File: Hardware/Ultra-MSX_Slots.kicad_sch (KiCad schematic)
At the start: 11 parts

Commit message: Finished the VDP-board, finished up the mixer-section, removed the buffer-pins from the FPGA, and instead added external buffers for the slots, designed a marquee-block with the Ultra-MSX logo, designed the logotype, andmultiple other changes.
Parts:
- added R17, R20, R21, R22, R23: R_RC0603FR-0710KL, LRJ:R_0603_1608Metric_roundcourt, symbol LRJ-parts:R_RC0603FR-0710KL
- added U14: SN74ABTH16244DL, Package_SO:TSSOP-56_6.1x14mm_P0.5mm, symbol LRJ-parts:SN74ABTH16244DL
- added U15: SN74ABT241APW, Package_SO:TSSOP-56_6.1x14mm_P0.5mm, symbol LRJ-parts:SN74ABT241APW
- added U6: 74ABT245PW_118, Package_SO:TSSOP-20_4.4x6.5mm_P0.65mm, symbol LRJ-parts:74ABT245PW_118
- R85, R86, R87, R88, R89, R90, R91, R92: footprint Resistor_SMD:R_0603_1608Metric_Pad0.98x0.95mm_HandSolder -> LRJ:R_0603_1608Metric_roundcourt
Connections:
- net +5V: now also R20.2
- net BA0: now also U14.2 (_{1}Y_{1})
- net BA1: now also U14.3 (_{1}Y_{2})
- net BA10: now also U14.16 (_{3}Y_{3})
- net BA11: now also U14.17 (_{3}Y_{4})
- net BA12: now also U14.19 (_{4}Y_{1})
- net BA13: now also U14.20 (_{4}Y_{2})
- net BA14: now also U14.22 (_{4}Y_{3})
- net BA15: now also U14.23 (_{4}Y_{4})
- net BA2: now also U14.5 (_{1}Y_{3})
- net BA3: now also U14.6 (_{1}Y_{4})
- net BA4: now also U14.8 (_{2}Y_{1})
- net BA5: now also U14.9 (_{2}Y_{2})
- net BA6: now also U14.11 (_{2}Y_{3})
- net BA7: now also U14.12 (_{2}Y_{4})
- net BA8: now also U14.13 (_{3}Y_{1})
- net BA9: now also U14.14 (_{3}Y_{2})
- net BD0: now also U6.2 (A0)
- net BD1: now also U6.3 (A1)
- net BD2: now also U6.4 (A2)
- net BD3: now also U6.5 (A3)
- net BD4: now also U6.6 (A4)
- net BD5: now also U6.7 (A5)
- net BD6: now also U6.8 (A6)
- net BD7: now also U6.9 (A7)
- net B_CLK: now also U15.3 (_{2}Y_{4})
- net GND: now also R17.2, R21.2, R22.2, R23.2, U14.24 (4~{OE}), U14.48 (2~{OE})
- net ~{B_IORQ}: now also U15.12 (_{1}Y_{4})
- net ~{B_M1}: now also U15.16 (_{1}Y_{2})
- net ~{B_MREQ}: now also U15.14 (_{1}Y_{3})
- net ~{B_RD}: now also U15.9 (_{2}Y_{1})
- net ~{B_RESET}: now also U15.5 (_{2}Y_{3})
- net ~{B_RFSH}: now also U15.18 (_{1}Y_{1})
- net ~{B_WR}: now also U15.7 (_{2}Y_{2})
- net SLT3_SND renamed SLT3_SND_L
- new net: R23.1, U14.25 (3~{OE})
- new net: R21.1, U6.19 (~{OE})
- new net: R17.1, U15.1 (1~{OE})
- new net: R22.1, U14.1 (1~{OE})
- new net: R20.1, U15.19 (2OE)
- new net A0: U14.47 (_{1}A_{1})
- new net A1: U14.46 (_{1}A_{2})
- new net A10: U14.33 (_{3}A_{3})
- new net A11: U14.32 (_{3}A_{4})
- new net A12: U14.30 (_{4}A_{1})
- new net A13: U14.29 (_{4}A_{2})
- new net A14: U14.27 (_{4}A_{3})
- new net A15: U14.26 (_{4}A_{4})
- new net A2: U14.44 (_{1}A_{3})
- new net A3: U14.43 (_{1}A_{4})
- new net A4: U14.41 (_{2}A_{1})
- new net A5: U14.40 (_{2}A_{2})
- new net A6: U14.38 (_{2}A_{3})
- new net A7: U14.37 (_{2}A_{4})
- new net A8: U14.36 (_{3}A_{1})
- new net A9: U14.35 (_{3}A_{2})
- new net CLK_BUS: U15.17 (_{2}A_{4})
- new net D0: U6.18 (B0)
- new net D1: U6.17 (B1)
- new net D2: U6.16 (B2)
- new net D3: U6.15 (B3)
- new net D4: U6.14 (B4)
- new net D5: U6.13 (B5)
- new net D6: U6.12 (B6)
- new net D7: U6.11 (B7)
- new net SLT_DIR: U6.1 (DIR)
- new net ~{IORQ}: U15.8 (_{1}A_{4})
- new net ~{M1}: U15.4 (_{1}A_{2})
- new net ~{MREQ}: U15.6 (_{1}A_{3})
- new net ~{RD}: U15.11 (_{2}A_{1})
- new net ~{RESET}: U15.15 (_{2}A_{3})
- new net ~{RFSH}: U15.2 (_{1}A_{1})
- new net ~{WR}: U15.13 (_{2}A_{2})
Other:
- note added: "Dual direction buffer"
- note removed: "Buffered Signals"
- moved on the sheet: R85, R86, R87, R88, R89, R90, R91, R92, SLOT1, SLOT2, SLOT3

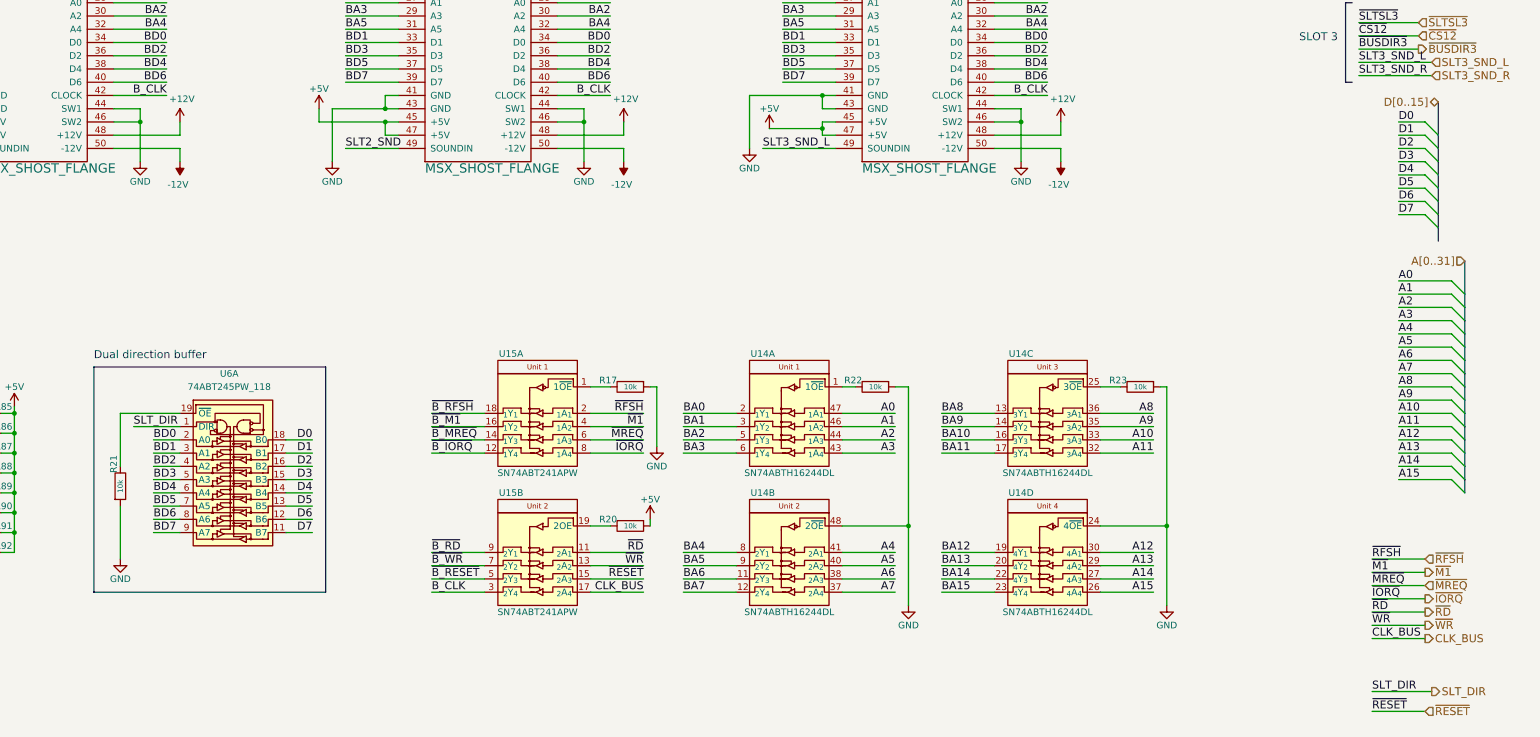
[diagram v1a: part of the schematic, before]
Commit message: Redesigned VDP-board to include a socket, increased it to 4 layers. Various clean-ups here and there. Improved the printer-port and joystick-port 3D-models. Improved the cooling-fin 3D-model, and added attachment-spring in 3D-model.
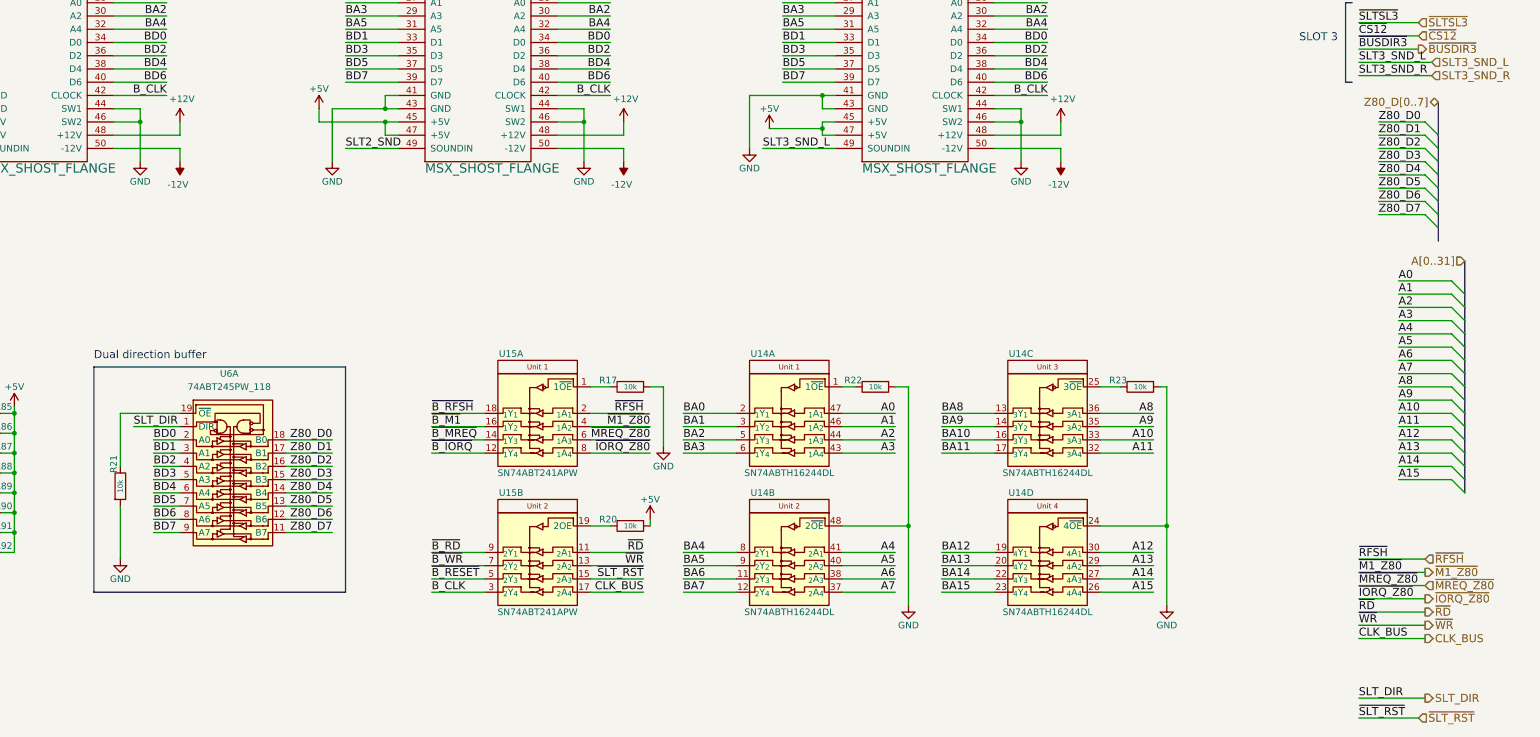
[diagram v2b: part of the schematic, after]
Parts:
- U14: footprint Package_SO:TSSOP-56_6.1x14mm_P0.5mm -> LRJ:Texas_R-PDSO-G48_7.7x16.0mm
- U15: footprint Package_SO:TSSOP-56_6.1x14mm_P0.5mm -> Package_SO:Texas_PWP0020A; MPN SN74ABTH16244DL -> SN74ABT241APW
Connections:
- net D0 renamed Z80_D0
- net D1 renamed Z80_D1
- net D2 renamed Z80_D2
- net D3 renamed Z80_D3
- net D4 renamed Z80_D4
- net D5 renamed Z80_D5
- net D6 renamed Z80_D6
- net D7 renamed Z80_D7
- net ~{IORQ} renamed ~{IORQ_Z80}
- net ~{M1} renamed ~{M1_Z80}
- net ~{MREQ} renamed ~{MREQ_Z80}
- net ~{RESET} renamed ~{SLT_RST}

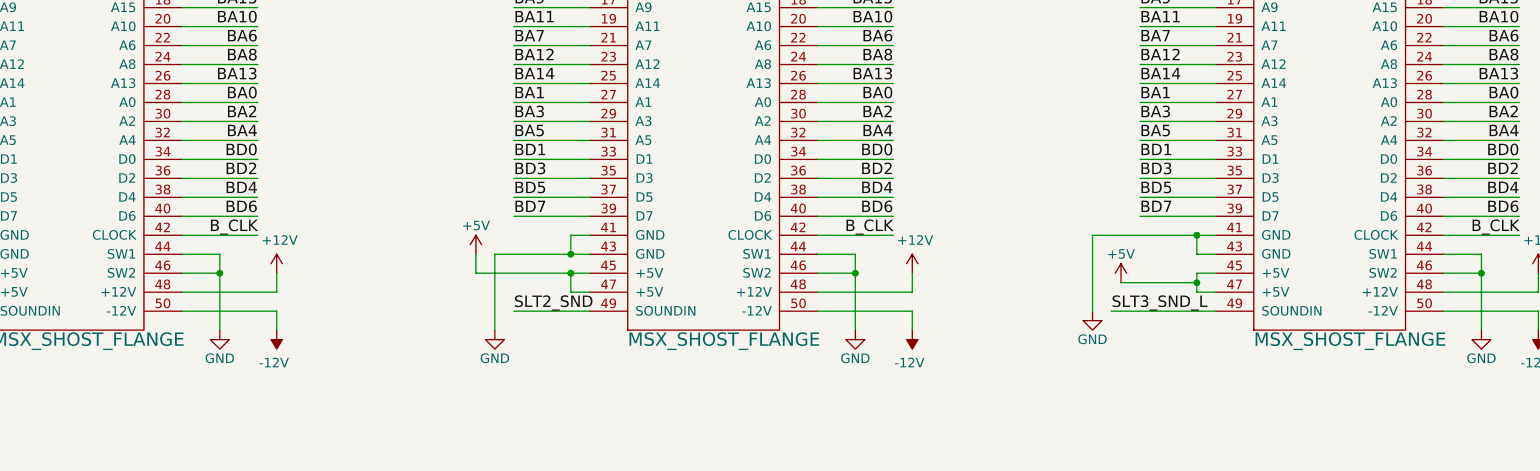
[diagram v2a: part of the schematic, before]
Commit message: Multiple redesigns of the IO-shield. Replaced FPGA with lower pin-count AT10K, since the higher pin-count one is now obsolete.
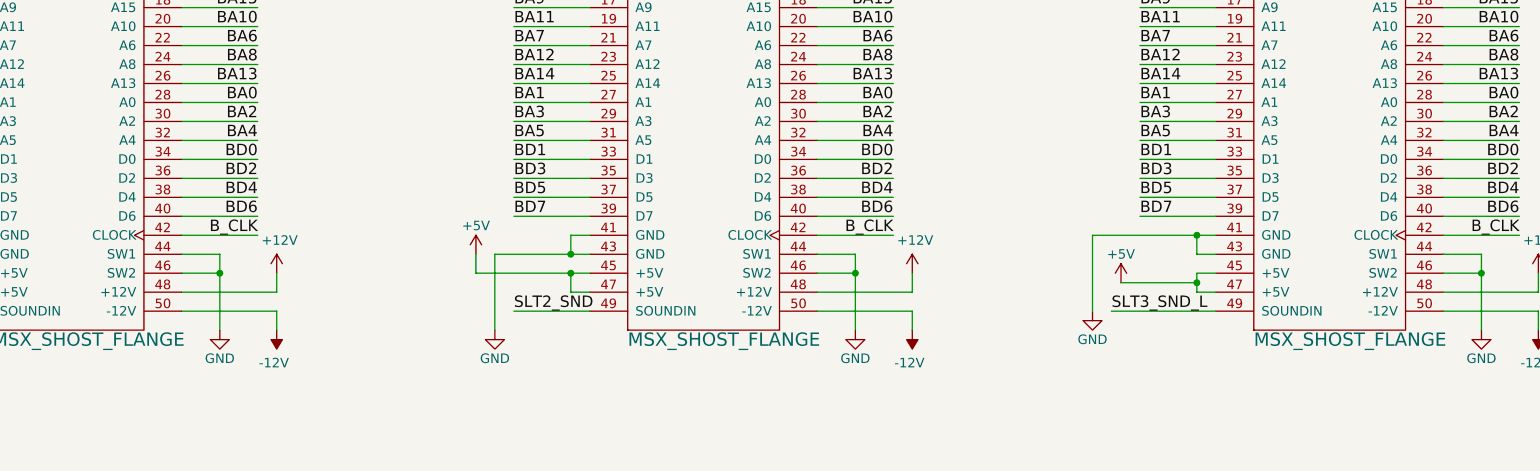
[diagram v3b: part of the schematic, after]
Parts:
- SLOT1, SLOT2, SLOT3: MPN (none) -> 5530841-5; Manufacturer (none) -> T.E Connectivity
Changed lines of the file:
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@@
     (effects (font (size 1.524 1.524)) (justify left))
   )
-  (symbol (lib_id "Ultra-MSX:MSX_SHOST_FLANGE") (at 124.46 59.69 0) (unit 1)
+  (symbol (lib_name "MSX_SHOST_FLANGE_1") (lib_id "Ultra-MSX:MSX_SHOST_FLANGE") (at 124.46 59.69 0) (unit 1)
     (in_bom yes) (on_board yes)
     (property "Reference" "SLOT1" (id 0) (at 114.3 25.4 0)
@@
     (property "Datasheet" "https://www.te.com/usa-en/product-5530843-5.datasheet.pdf" (id 3) (at 127 67.31 0)
       (effects (font (size 1.524 1.524)) hide)
+    )
+    (property "Manufacturer" "T.E Connectivity" (id 4) (at 152.4 49.53 0)
+      (effects (font (size 1.27 1.27)) hide)
+    )
+    (property "MPN" "5530841-5" (id 5) (at 149.86 52.07 0)
+      (effects (font (size 1.27 1.27)) hide)
     )
     (pin "1")
@@
     (pin "1")
   )
-  (symbol (lib_id "Ultra-MSX:MSX_SHOST_FLANGE") (at 209.55 59.69 0) (unit 1)
+  (symbol (lib_name "MSX_SHOST_FLANGE_2") (lib_id "Ultra-MSX:MSX_SHOST_FLANGE") (at 209.55 59.69 0) (unit 1)
     (in_bom yes) (on_board yes)
     (property "Reference" "SLOT2" (id 0) (at 199.39 25.4 0)
@@
     (property "Datasheet" "https://www.te.com/usa-en/product-5530843-5.datasheet.pdf" (id 3) (at 212.09 67.31 0)
       (effects (font (size 1.524 1.524)) hide)
+    )
+    (property "Manufacturer" "T.E Connectivity" (id 4) (at 237.49 49.53 0)
+      (effects (font (size 1.27 1.27)) hide)
+    )
+    (property "MPN" "5530841-5" (id 5) (at 234.95 52.07 0)
+      (effects (font (size 1.27 1.27)) hide)
     )
     (pin "1")
@@
       (effects (font (size 1.524 1.524)) hide)
     )
-    (pin "1")
+    (property "Manufacturer" "T.E Connectivity" (id 4) (at 321.31 49.53 0)
+      (effects (font (size 1.27 1.27)) hide)
+    )
+    (property "MPN" "5530841-5" (id 5) (at 318.77 52.07 0)
+      (effects (font (size 1.27 1.27)) hide)
+    )
+    (pin "1")

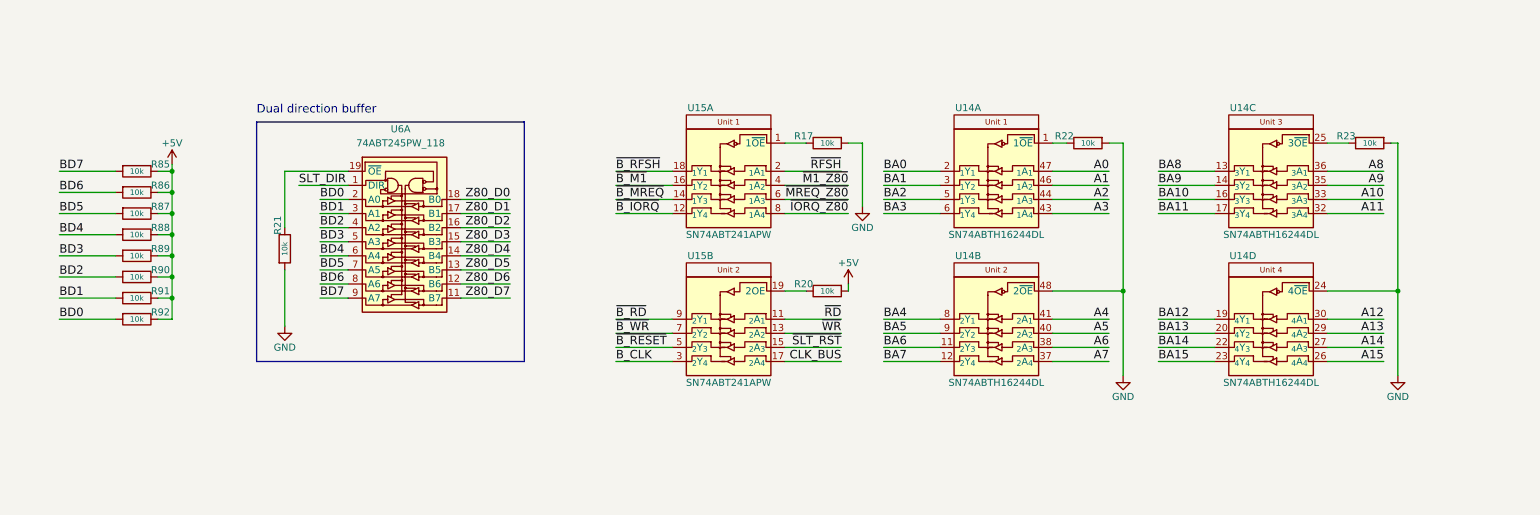
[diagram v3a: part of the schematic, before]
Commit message: Added cooler and CPU-mount footprints, as well as Indication LEDs.
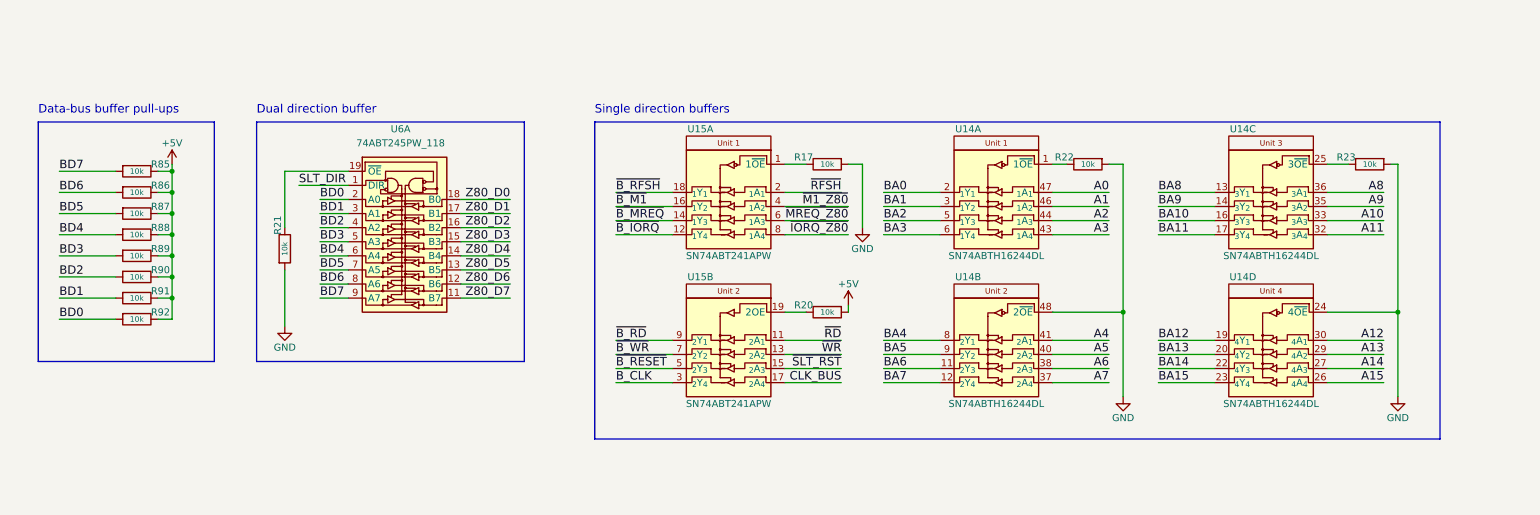
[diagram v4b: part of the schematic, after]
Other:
- note added: "Data-bus buffer pull-ups"
- note added: "Single direction buffers"
- moved on the sheet: R17, R20, R22, R23, U14A, U14B, U14C, U14D, U15A, U15B

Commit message: Started fixing many small issues.
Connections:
- net ~{CS12} renamed ~{SLT_CS12}
- net ~{CS1} renamed ~{SLT_CS1}
- net ~{CS2} renamed ~{SLT_CS2}
